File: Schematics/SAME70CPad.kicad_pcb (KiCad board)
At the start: 4 copper layers, 100 x 75 mm, 246 parts, among them J1 ER-TFTMO70-5-LCD, J10 Headset, J11 MIC_IN, J12 POWER, J13 RESET, J14 BATTERY, J15 PWR_QON, J2 nFL24l02_Module, J3 SWD/JTAG, J4 USB_OTG, J5 DEBUG_UART, J6 ERASE, J7 POWER_IN, J8 SPKRL, J9 SPKRR, M1 MountingHole, M2 MountingHole, M3 MountingHole, M4 MountingHole, P1 ESP-12E, P2 ER-TFTMO70-5-SD, P3 MicroSD, Q1 RE1C002UN, Q2 RE1C002UN, Q3 RE1C002UN, SW1 SW_POWER, U1 IS42S16320D, U10 XC9142B50DMR-G, U11 TPS62063, U12 AP2138N18, U13 bq24297, U14 INA3221AIRGVx, U2 MCP1501T-25E/CHY, U3 IS25LP256D, U4 ATSAME70QxxA-AN, U5 D5V0F4U6SO, U6 TLV320AIC3111, U7 BME280, U8 MPU-9250, U9 ICS-40181, Y1 32.768kHz, Y2 12MHz

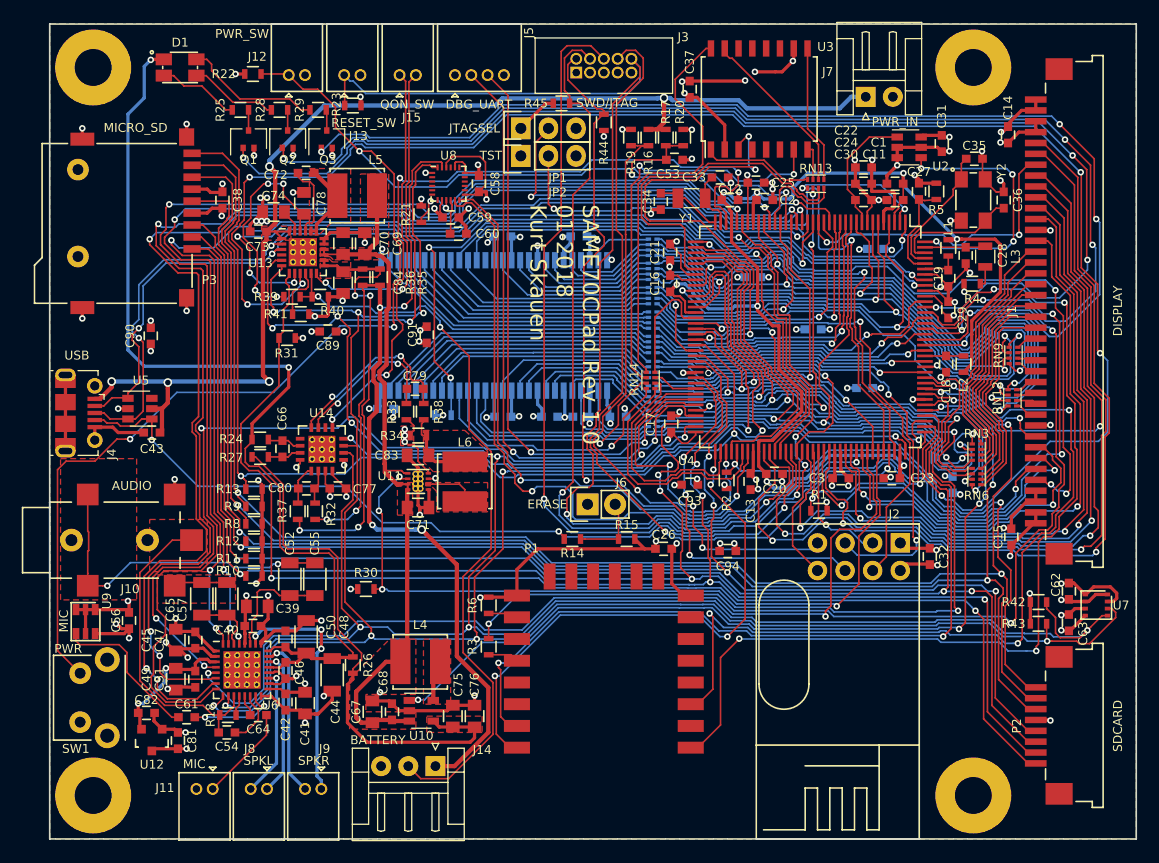
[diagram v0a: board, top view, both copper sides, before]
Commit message: Added some missing pullup resistors plus misc cleanup and optimization of the layout.
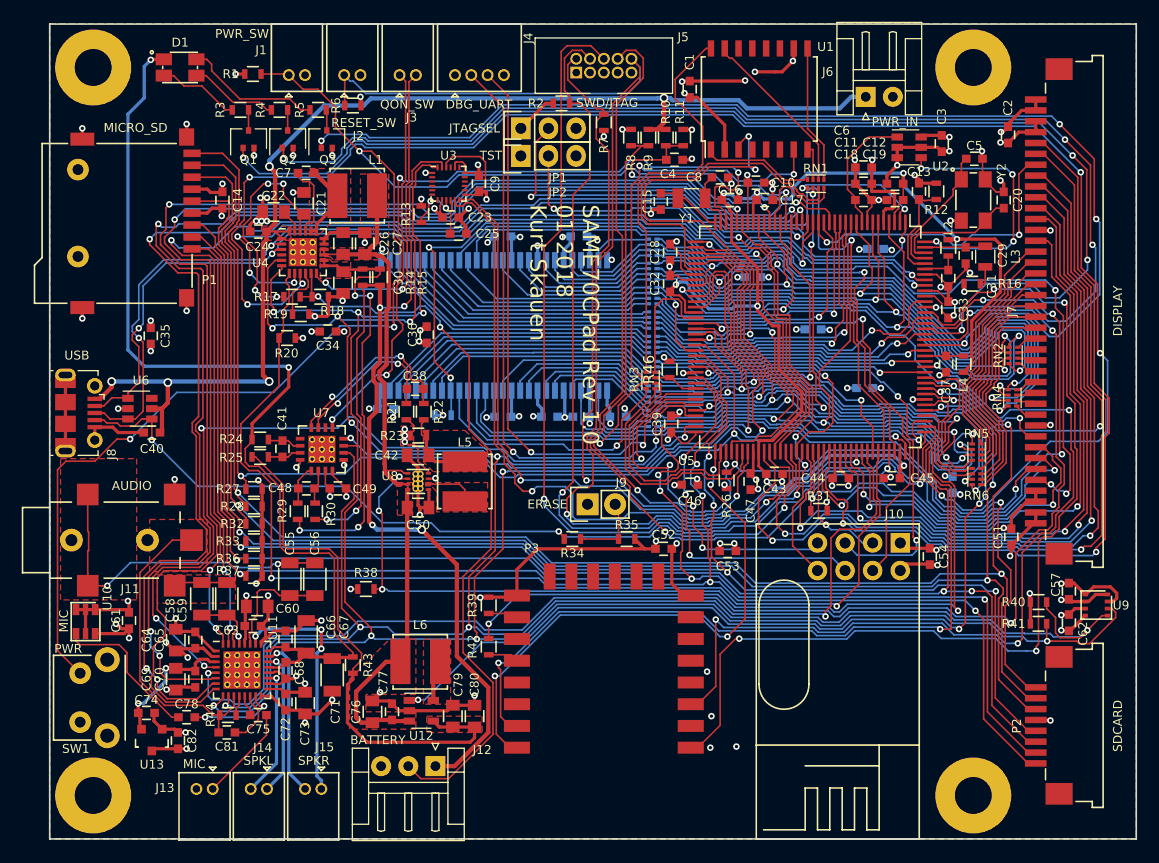
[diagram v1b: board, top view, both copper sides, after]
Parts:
- added R46: 100k, MyResistors:R_0603, F.Cu at (186.1, 102.8)
- renumbered C37 to C1, C25 to C10, C24 to C11, C1 to C12, C27 to C13, C38 to C14, C34 to C15, C12 to C16, C2 to C17, C30 to C18, C11 to C19, C14 to C2, C36 to C20, C78 to C21, C74 to C22, C59 to C23, C73 to C24, C60 to C25, C70 to C26, C69 to C27, C21 to C28, C28 to C29, C31 to C3, C84 to C30, C19 to C31, C16 to C32, C29 to C33, C89 to C34, C90 to C35, C91 to C36, C18 to C37, C79 to C38, C17 to C39, C53 to C4, C43 to C40, C66 to C41, C83 to C42, C20 to C43, C3 to C44, C23 to C45, C93 to C46, C13 to C47, C80 to C48, C77 to C49, C35 to C5, C71 to C50, C15 to C51, C26 to C52, C94 to C53, C32 to C54, C52 to C55, C55 to C56, C62 to C57, C65 to C58, C57 to C59, C22 to C6, C39 to C60, C56 to C61, C63 to C62, C40 to C63, C45 to C64, C47 to C65, C50 to C66, C48 to C67, C46 to C68, C49 to C69, C72 to C7, C51 to C70, C44 to C71, C42 to C72, C41 to C73, C82 to C74, C64 to C75, C67 to C76, C68 to C77, C61 to C78, C75 to C79, C33 to C8, C76 to C80, C54 to C81, C81 to C82, C5 to C83, C4 to C84, C87 to C85, C88 to C86, C85 to C87, C86 to C88, C10 to C89, C58 to C9, C6 to C90, C7 to C91, C8 to C92, C9 to C93, C92 to C94, J12 to J1, J2 to J10, J10 to J11, J14 to J12, J11 to J13, J8 to J14, J9 to J15, J13 to J2, J15 to J3, J5 to J4, J3 to J5, J7 to J6, J1 to J7, J4 to J8, J6 to J9, L5 to L1, L1 to L2, L2 to L4, L6 to L5, L4 to L6, M4 to M1, M3 to M2, M1 to M3, M2 to M4, P3 to P1, P1 to P3, R22 to R1, R17 to R10, R20 to R11, R5 to R12, R21 to R13, R36 to R14, R35 to R15, R4 to R16, R39 to R17, R40 to R18, R41 to R19, R45 to R2, R31 to R20, R33 to R21, R38 to R22, R34 to R23, R27 to R25, R2 to R26, R13 to R27, R9 to R28, R37 to R29, R25 to R3, R32 to R30, R1 to R31, R8 to R32, R12 to R33, R14 to R34, R15 to R35, R11 to R36, R10 to R37, R30 to R38, R6 to R39, R28 to R4, R42 to R40, R43 to R41, R3 to R42, R26 to R43, R18 to R44, R7 to R45, R29 to R5, R23 to R6, R44 to R7, R19 to R8, R16 to R9, RN13 to RN1, RN7 to RN10, RN4 to RN11, RN1 to RN12, RN5 to RN13, RN2 to RN14, RN9 to RN2, RN14 to RN3, RN12 to RN4, RN3 to RN5, RN11 to RN7, RN10 to RN9, U3 to U1, U9 to U10, U6 to U11, U10 to U12, U12 to U13, U1 to U14, U8 to U3, U13 to U4, U4 to U5, U5 to U6, U14 to U7, U11 to U8, U7 to U9
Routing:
- net Earth: track 898.1 -> 928.5 mm, vias 100 -> 104
- net +3V3: track 623.3 -> 630.9 mm, vias 59 -> 60
- net AUDIO_DIN: track 85.3 -> 86.3 mm
- net WIFI_RESET: track 90.4 -> 91.2 mm
- net SDRAM_BANK1: track 25.1 -> 25.9 mm
- net WIFI_EN: track 79.1 -> 78.3 mm
- net I2CBUS2_SCL: track 217.5 -> 218.2 mm
- net WIFI_FLASH: track 96.1 -> 96.7 mm
- net AB13: track 26.8 -> 26.2 mm
- net QSPI_SCK: track 10.9 -> 11.5 mm
- net PWR_5VEN: track 81.9 -> 82.5 mm
- net I2CBUS2_SDA: track 228.4 -> 229.0 mm

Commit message: - Annotated components geographically from the PCB layout. - Added the OSHW logo to the PCB. - Some minor layout cleanup.
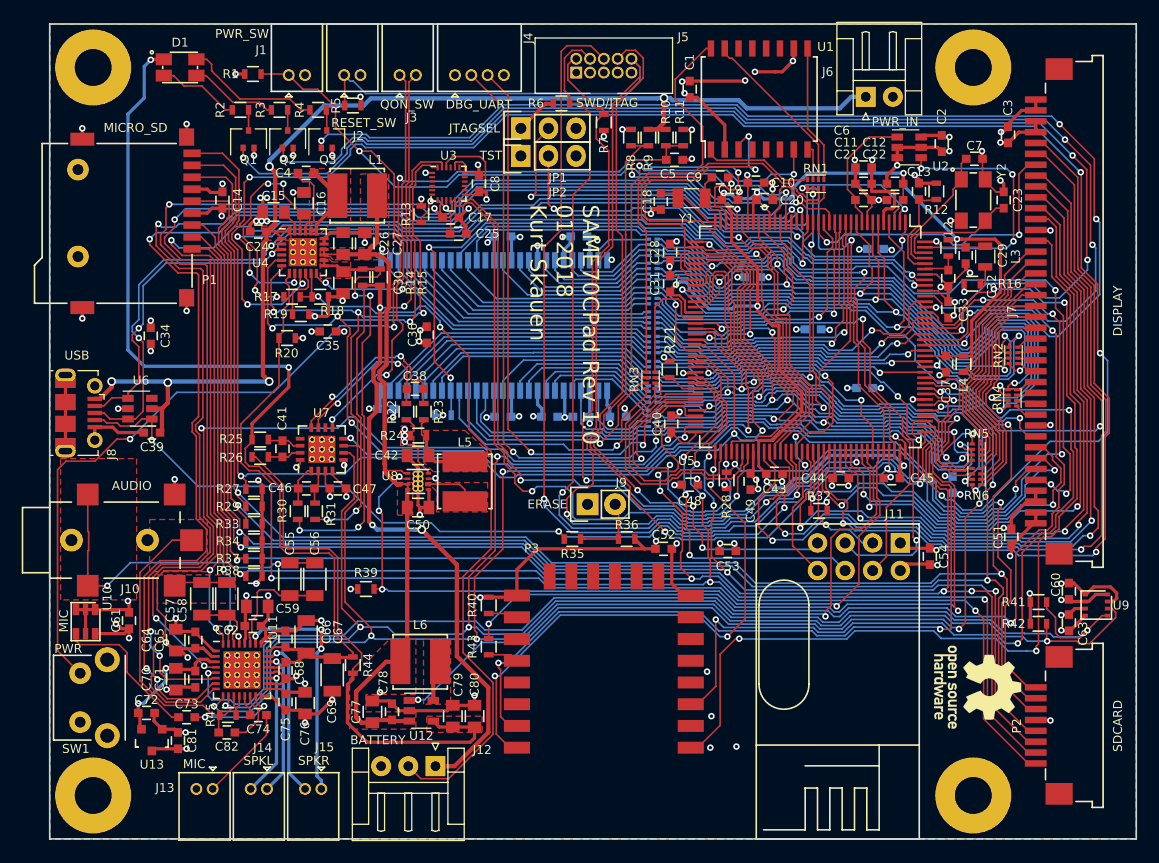
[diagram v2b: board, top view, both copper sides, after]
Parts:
- added REF***: OSHW-Logo_7.5x8mm_SilkScreen, Symbols:OSHW-Logo_7.5x8mm_SilkScreen, F.Cu at (214.4, 132.0)
- renumbered C22 to C15, C21 to C16, C23 to C17, C15 to C18, C16 to C19, C3 to C2, C17 to C20, C18 to C21, C19 to C22, C20 to C23, C2 to C3, C32 to C31, C31 to C32, C35 to C34, C34 to C35, C40 to C39, C7 to C4, C39 to C40, C48 to C46, C49 to C47, C46 to C48, C47 to C49, C4 to C5, C58 to C57, C59 to C58, C60 to C59, C57 to C60, C63 to C62, C62 to C63, C71 to C69, C5 to C7, C69 to C70, C70 to C71, C74 to C72, C78 to C73, C75 to C74, C72 to C75, C73 to C76, C76 to C77, C77 to C78, C9 to C8, C82 to C81, C81 to C82, C8 to C9, J11 to J10, J10 to J11, R3 to R2, R46 to R21, R21 to R22, R22 to R23, R23 to R24, R24 to R25, R25 to R26, R26 to R28, R28 to R29, R4 to R3, R29 to R30, R30 to R31, R31 to R32, R32 to R33, R33 to R34, R34 to R35, R35 to R36, R36 to R37, R37 to R38, R38 to R39, R5 to R4, R39 to R40, R40 to R41, R41 to R42, R42 to R43, R43 to R44, R44 to R45, R45 to R46, R6 to R5, R2 to R6
